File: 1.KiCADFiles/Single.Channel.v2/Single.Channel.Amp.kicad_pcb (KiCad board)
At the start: 4 copper layers, 20 x 60 mm, 18 parts, among them J2 Conn_01x08, J3 Conn_01x04, J4 Conn_Coaxial_In, J5 Conn_Coaxial_Out, Q1 MMBT3904, Q2 MMBT3906

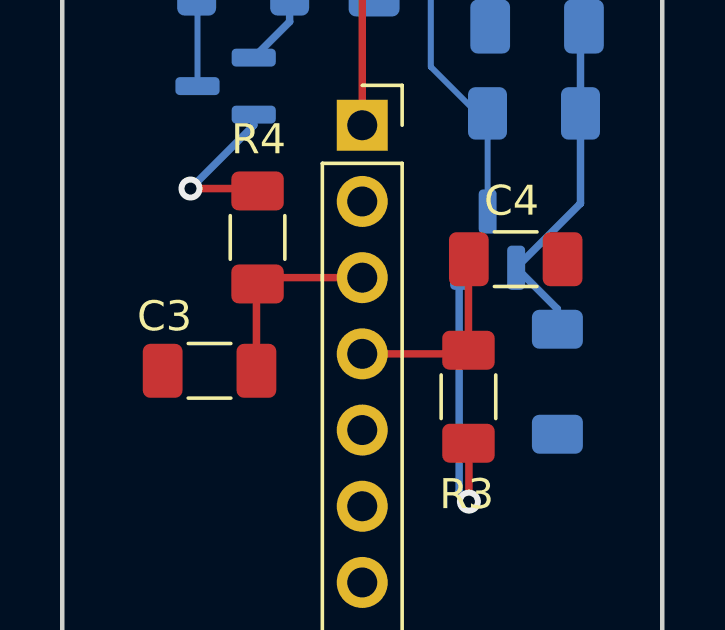
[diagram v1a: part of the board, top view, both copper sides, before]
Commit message: Updated Voltage Reference Points
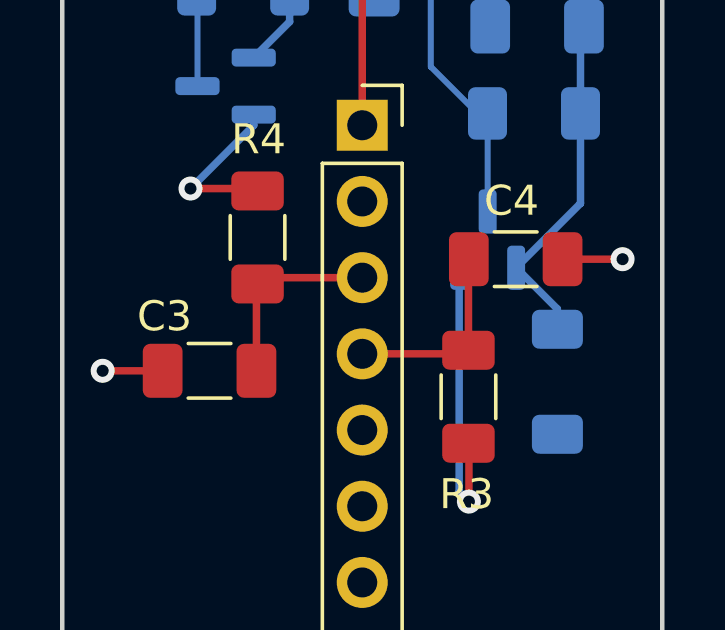
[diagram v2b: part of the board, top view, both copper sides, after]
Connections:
- C3 pad 2: GND1 -> GND
- C4 pad 2: GND1 -> GND
- J4 pad 2: GND -> GND1
- J5 pad 2: GND -> GND1
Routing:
- net GND: track 0.00 -> 4.00 mm, vias 0 -> 2
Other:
- board text added: "Single Channel v.2.1 June 2023 Alfredo Barajas Enriquez"
- board text removed: "Single Channel v.2 June 2023 Alfredo Barajas Enriquez"
